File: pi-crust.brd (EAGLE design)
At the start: 43.7 x 40.4 mm, 11 parts

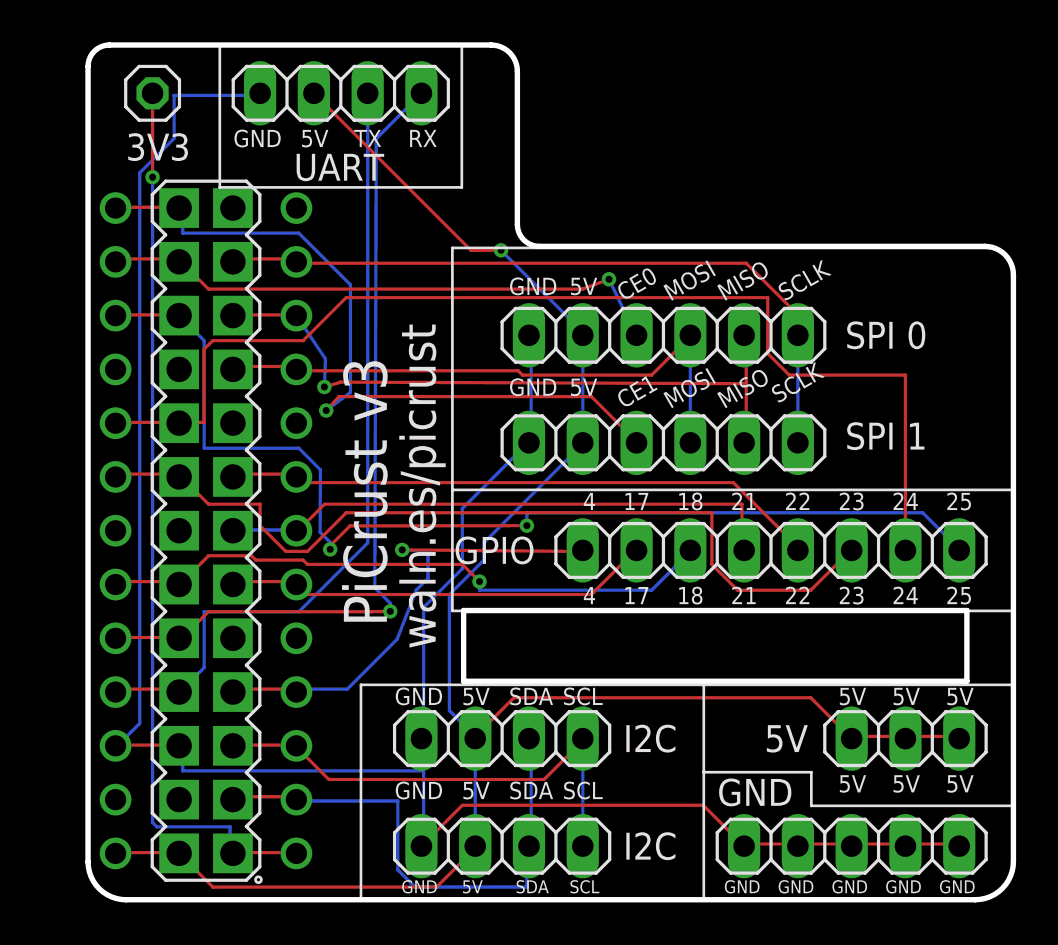
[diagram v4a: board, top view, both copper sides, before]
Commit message: V4: Replaced single 3V3 header with a double. Actually makes it cheaper to make and a 2nd connector is always handy. Shuffled the UART along a little.
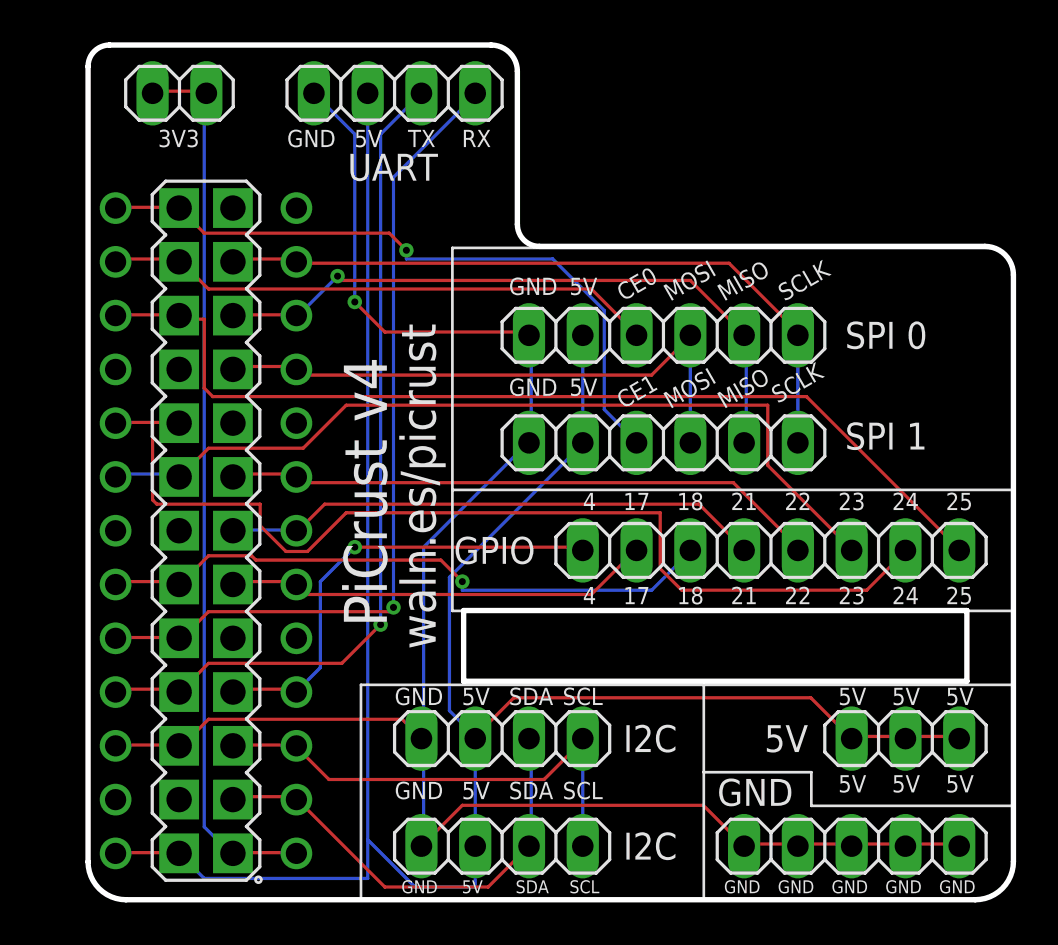
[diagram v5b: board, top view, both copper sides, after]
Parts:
- JP4: value 3V3 -> (none); device pinhead:1X01 -> pinhead:1X02
- moved JP6 2.54 mm to (16.5, 38.1)
- moved JP4 1.27 mm to (6.35, 38.1)
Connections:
- net 3V3: now also JP4.2
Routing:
- net 5V: track 88.0 -> 109.4 mm, vias 1 -> 0
- net GND: track 105.5 -> 88.7 mm, vias 0 -> 1
- net GPIO_25: track 51.3 -> 46.4 mm, vias 2 -> 0
- net GPIO_24: track 53.1 -> 48.5 mm
- net SPI_CE_1: track 35.6 -> 32.2 mm
- net I2C_SDA: track 24.8 -> 21.8 mm
- net UART_TX: track 37.8 -> 39.9 mm, vias 0 -> 1
- net GPIO_04: track 23.3 -> 22.1 mm
- net GPIO_21: track 26.8 -> 25.6 mm
- net SPI_CE_0: track 27.0 -> 26.2 mm, vias 1 -> 0
- net SPI_MISO: track 31.9 -> 31.3 mm
- net GPIO_23: track 41.4 -> 40.9 mm
- net 3V3: track 42.6 -> 42.3 mm, vias 1 -> 0
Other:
- board text added: "3V3"
- board text added: "PiCrust v4"
- board text removed: "PiCrust v3"

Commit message: Changed shape of hole to accomodate new DSI connector cover on RPi rev 2.
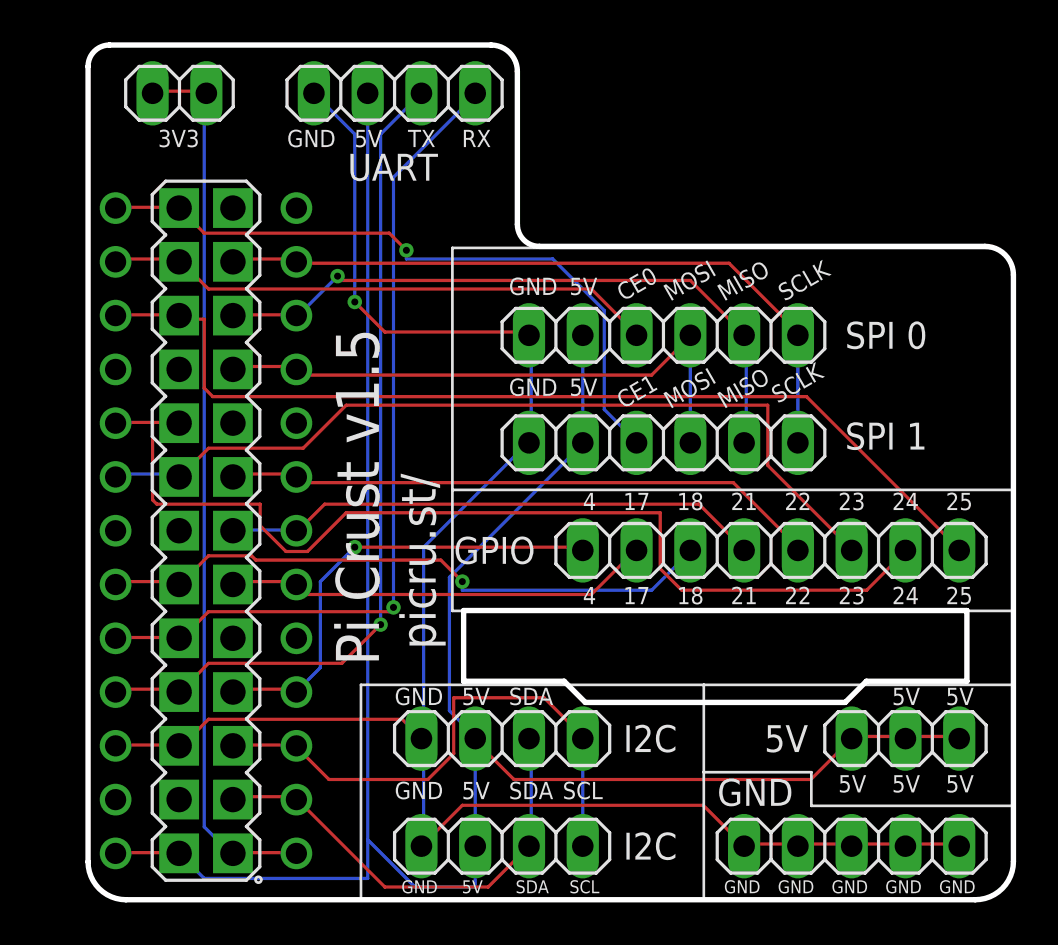
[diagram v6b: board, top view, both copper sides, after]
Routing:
- net I2C_SCL: track 23.2 -> 26.3 mm
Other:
- outline, holes or cut-outs redrawn
- board text added: "Pi Crust v1.5"
- board text added: "by @joewalnes (CC-SA)"
- board text added: "picru.st/"
- board text removed: "PiCrust v4"
- board text removed: "Think inside the box"
- board text removed: "waln.es/picrust"
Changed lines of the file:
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@@
 <setting verticaltext="up"/>
 </settings>
-<grid distance="0.05" unitdist="inch" unit="inch" style="lines" multiple="1" display="yes" altdistance="0.025" altunitdist="inch" altunit="inch"/>
+<grid distance="0" unitdist="inch" unit="inch" style="lines" multiple="1" display="yes" altdistance="0.025" altunitdist="inch" altunit="inch"/>
 <layers>
 <layer number="1" name="Top" color="4" fill="1" visible="yes" active="yes"/>
@@
 <wire x1="2.032" y1="1.7989" x2="2.032" y2="39.37" width="0.254" layer="20"/>
 <wire x1="19.772" y1="10.34" x2="19.772" y2="13.68" width="0" layer="20"/>
-<wire x1="19.772" y1="10.33" x2="43.542" y2="10.33" width="0.254" layer="20"/>
 <wire x1="43.542" y1="10.33" x2="43.542" y2="13.67" width="0.254" layer="20"/>
 <wire x1="43.542" y1="13.67" x2="19.772" y2="13.67" width="0.254" layer="20"/>
@@
 <text x="19.685" y="9.2075" size="0.8128" layer="25">5V</text>
 <text x="19.685" y="4.7625" size="0.8128" layer="25">5V</text>
-<text x="37.465" y="9.2075" size="0.8128" layer="25">5V</text>
 <text x="40.005" y="9.2075" size="0.8128" layer="25">5V</text>
 <text x="42.545" y="9.2075" size="0.8128" layer="25">5V</text>
@@
 <text x="21.9075" y="9.2075" size="0.8128" layer="25">SDA</text>
 <text x="21.9075" y="4.7625" size="0.8128" layer="25">SDA</text>
-<text x="24.4475" y="9.2075" size="0.8128" layer="25">SCL</text>
 <text x="24.4475" y="4.7625" size="0.8128" layer="25">SCL</text>
 <text x="16.8275" y="0.3175" size="0.6096" layer="25">GND</text>
@@
 <rectangle x1="9.85" y1="4.47" x2="15.96" y2="14.98" layer="40"/>
 <rectangle x1="37.75" y1="23.39" x2="45.29" y2="27.7" layer="40"/>
-<rectangle x1="31.52" y1="7" x2="35.02" y2="9.84" layer="40"/>
+<rectangle x1="31.52" y1="7" x2="35.02" y2="9.332" layer="40"/>
 <rectangle x1="27.15" y1="1.14" x2="29.94" y2="5.16" layer="40"/>
 <rectangle x1="12.3477" y1="16.9706" x2="18.2779" y2="36.1728" layer="40"/>
 <rectangle x1="42.418" y1="20.828" x2="43.942" y2="22.352" layer="26"/>
 <rectangle x1="28.194" y1="6.604" x2="29.718" y2="8.128" layer="26"/>
-<text x="16.146478125" y="12.89490625" size="2.032" layer="25" font="vector" ratio="12" rot="R90">PiCrust v4</text>
-<text x="18.4519875" y="11.83216875" size="1.651" layer="25" font="vector" rot="R90">waln.es/picrust</text>
-<text x="14.08355" y="8.7385875" size="1.27" layer="26" font="vector" rot="MR90">Think inside the box</text>
+<text x="15.771271875" y="11.068684375" size="2.032" layer="25" font="vector" ratio="12" rot="R90">Pi Crust v1.5</text>
+<text x="18.4519875" y="11.83216875" size="1.651" layer="25" font="vector" rot="R90">picru.st/</text>
+<text x="14.08355" y="1.54111875" size="1.27" layer="26" font="vector" rot="MR90">by @joewalnes (CC-SA) </text>
 <wire x1="10.16" y1="40.386" x2="10.16" y2="33.528" width="0.127" layer="27"/>
 <wire x1="10.16" y1="33.528" x2="22.352" y2="33.528" width="0.127" layer="27"/>
 <text x="5.334" y="35.56" size="0.8128" layer="25">3V3</text>
+<wire x1="19.772" y1="10.33" x2="24.5196" y2="10.33" width="0.254" layer="20"/>
+<wire x1="24.5196" y1="10.33" x2="25.5196" y2="9.33" width="0.254" layer="20"/>
+<wire x1="25.5196" y1="9.33" x2="37.7944" y2="9.33" width="0.254" layer="20"/>
+<wire x1="37.7944" y1="9.33" x2="38.7944" y2="10.33" width="0.254" layer="20"/>
+<wire x1="38.7944" y1="10.33" x2="43.542" y2="10.33" width="0.254" layer="20"/>
 </plain>
 <attributes>
@@
 <wire x1="15.24" y1="2.8448" x2="15.24" y2="1.016" width="0.1524" layer="16"/>
 <wire x1="6.5024" y1="2.032" x2="6.3343" y2="2.1998" width="0.1524" layer="16"/>
-<wire x1="36.1696" y1="9.5504" x2="38.1" y2="7.62" width="0.1524" layer="1"/>
-<wire x1="22.1488" y1="9.5504" x2="36.1696" y2="9.5504" width="0.1524" layer="1"/>
-<wire x1="20.32" y1="7.7216" x2="22.1488" y2="9.5504" width="0.1524" layer="1"/>
-<wire x1="20.32" y1="7.7216" x2="20.32" y2="7.62" width="0.1524" layer="1"/>
+<wire x1="36.1696" y1="5.6896" x2="38.1" y2="7.62" width="0.1524" layer="1"/>
+<wire x1="22.1488" y1="5.6896" x2="36.1696" y2="5.6896" width="0.1524" layer="1"/>
+<wire x1="20.32" y1="7.5184" x2="22.1488" y2="5.6896" width="0.1524" layer="1"/>
+<wire x1="20.32" y1="7.5184" x2="20.32" y2="7.62" width="0.1524" layer="1"/>
 <wire x1="19.1008" y1="15.24" x2="25.4" y2="21.5392" width="0.1524" layer="16"/>
 <wire x1="19.1008" y1="8.9408" x2="19.1008" y2="15.24" width="0.1524" layer="16"/>
@@
 <wire x1="25.4" y1="7.62" x2="25.4" y2="2.54" width="0.1524" layer="16"/>
 <wire x1="13.4112" y1="5.6896" x2="11.9888" y2="7.112" width="0.1524" layer="1"/>
-<wire x1="23.5712" y1="5.6896" x2="13.4112" y2="5.6896" width="0.1524" layer="1"/>
-<wire x1="25.4" y1="7.5184" x2="23.5712" y2="5.6896" width="0.1524" layer="1"/>
+<wire x1="18.0848" y1="5.6896" x2="13.4112" y2="5.6896" width="0.1524" layer="1"/>
+<wire x1="19.304" y1="6.9088" x2="18.0848" y2="5.6896" width="0.1524" layer="1"/>
+<wire x1="19.304" y1="9.5504" x2="19.304" y2="6.9088" width="0.1524" layer="1"/>
+<wire x1="23.5712" y1="9.5504" x2="19.304" y2="9.5504" width="0.1524" layer="1"/>
+<wire x1="25.4" y1="7.7216" x2="23.5712" y2="9.5504" width="0.1524" layer="1"/>
 <wire x1="11.9888" y1="7.112" x2="11.87288125" y2="7.278196875" width="0.1524" layer="1"/>
-<wire x1="25.4" y1="7.5184" x2="25.4" y2="7.62" width="0.1524" layer="1"/>
+<wire x1="25.4" y1="7.7216" x2="25.4" y2="7.62" width="0.1524" layer="1"/>
 </signal>
 <signal name="SPI_CE_0">
@@
 </signal>
 </signals>
+<errors>
+</errors>
 </board>
 </drawing>
